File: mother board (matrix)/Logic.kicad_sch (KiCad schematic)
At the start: 1 part, among them U1 STM32F030C6Tx

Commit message: changes
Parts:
- added C1, C2, C3, C4: 100n, symbol Device:C
- added C304, C305: 20p, Capacitor_SMD:C_0603_1608Metric_Pad1.08x0.95mm_HandSolder, symbol Device:C_Small
- added C306, C308: 10u, Capacitor_Tantalum_SMD:CP_EIA-6032-28_Kemet-C_Pad2.25x2.35mm_HandSolder, symbol Device:C_Polarized_Small
- added C307, C309: 100n, Capacitor_SMD:C_0603_1608Metric_Pad1.08x0.95mm_HandSolder, symbol Device:C_Small
- added D1, D2: D_TVS, symbol Device:D_TVS
- added D332: Green, LED_SMD:LED_0805_2012Metric_Pad1.15x1.40mm_HandSolder, symbol Device:LED_Small
- added D333: Red, LED_SMD:LED_0805_2012Metric_Pad1.15x1.40mm_HandSolder, symbol Device:LED_Small
- added J301: RS485, Connector_PinSocket_2.54mm:PinSocket_1x03_P2.54mm_Vertical_SMD_Pin1Right, symbol Connector_Generic:Conn_01x03
- added J304: SWD, Connector_PinSocket_2.54mm:PinSocket_1x04_P2.54mm_Vertical_SMD_Pin1Right, symbol Connector_Generic:Conn_01x04
- added J305: BOOT_TO/ SELECTOR, Connector_PinHeader_2.54mm:PinHeader_1x03_P2.54mm_Vertical_SMD_Pin1Left, symbol Connector_Generic:Conn_01x03
- added J311: BOOT_TO/ SELECTOR, Connector_PinHeader_2.54mm:PinHeader_1x02_P2.54mm_Vertical_SMD_Pin1Left, symbol Connector_Generic:Conn_01x02
- added R1, R2: 10, symbol Device:R
- added R3: 120, symbol Device:R
- added R301, R305, R309, R310, R311: 10k, Resistor_SMD:R_0603_1608Metric_Pad0.98x0.95mm_HandSolder, symbol Device:R_Small
- added R312: 510, Resistor_SMD:R_0603_1608Metric_Pad0.98x0.95mm_HandSolder, symbol Device:R_Small
- added R313: 680, Resistor_SMD:R_0603_1608Metric_Pad0.98x0.95mm_HandSolder, symbol Device:R_Small
- added R4: 360, symbol Device:R
- added SW301: SW_SPST, Button_Switch_SMD:SW_SPST_EVQPE1, symbol Switch:SW_SPST
- added U2: SN65HVD11HD, Package_SO:SOIC-8_3.9x4.9mm_P1.27mm, symbol Interface_UART:SN65HVD11HD
- added U302: LM1117-3.3, Package_TO_SOT_SMD:SOT-223, symbol Regulator_Linear:LM1117-3.3
- added Y301: 8 MHz, Crystal:Crystal_SMD_Abracon_ABM3C-4Pin_5.0x3.2mm, symbol Device:Crystal_Small
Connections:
- net at U1.1 (VDD): now also U1.24 (VDD), U1.48 (VDD), U1.9 (VDDA), C1.1, C2.1, C3.1, C4.1
- net GNDD: now reaches U1.23 (VSS), U1.47 (VSS)
- net GNDD: now also U1.8 (VSSA), C1.2, C2.2, C3.2, C304.1, C305.1, C306.2, C307.2, C308.2, C309.2, C4.2, D1.2 (A2), D2.2 (A2), D332.1 (K), D333.1 (K), J301.1 (Pin_1), J304.1 (Pin_1), J305.1 (Pin_1), J311.2 (Pin_2), R310.2, R311.2, R4.2, SW301.1 (A), U302.1 (GND), Y301.2 (GND), Y301.4 (GND)
- new net: C305.2, Y301.1
- new net: D1.1 (A1), J301.3 (Pin_3), R1.1, R3.1, R4.1
- new net: D2.1 (A1), J301.2 (Pin_2), R2.1, R3.2
- new net: J305.2 (Pin_2), R301.2
- new net: D333.2 (A), R313.2
- new net: D332.2 (A), R312.2
- new net +3.3V: C307.1, C308.1, C309.1, J304.4 (Pin_4), J305.3 (Pin_3), R305.1, R309.1, U302.2 (VO), U302.4 (VO)
- new net +5V: C306.1, J311.1 (Pin_1), U302.3 (VI)
- new net BOOT0: R301.1
- new net DE: R311.1
- new net LED_debug1: R312.1
- new net LED_debug2: R313.1
- new net RST: R305.2, SW301.2 (B)
- new net SWD_CLK: J304.2 (Pin_2)
- new net SWD_O: J304.3 (Pin_3)
- new net UART1_RX_R: R309.2
- new net Xtal_IN: C304.2, Y301.3
- new net ~{RE}: R310.1
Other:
- note added: "3.3V Regulation"
- note added: "DB BOOT SELECTOR"
- note added: "DB ICSP"
- note added: "DB Supply"
- note added: "Debug_LED"
- note added: "Doughter Board (LOGICAL BOARD)"
- note added: "INNY SYMBOL BYL, NIE WIEM CZY TEN NA PEWNO MOZE BYC"
- note added: "MCU"
- note added: "POWER DECOUPLING"
- note added: "max ESR 22 Ohm"
- moved on the sheet: U1

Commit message: matrix done
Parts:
- removed C1, C2, C3, C4: 100n, symbol Device:C
- removed C304, C305: 20p, Capacitor_SMD:C_0603_1608Metric_Pad1.08x0.95mm_HandSolder, symbol Device:C_Small
- removed C306, C308: 10u, Capacitor_Tantalum_SMD:CP_EIA-6032-28_Kemet-C_Pad2.25x2.35mm_HandSolder, symbol Device:C_Polarized_Small
- removed C307, C309: 100n, Capacitor_SMD:C_0603_1608Metric_Pad1.08x0.95mm_HandSolder, symbol Device:C_Small
- removed D1, D2: D_TVS, symbol Device:D_TVS
- removed D332: Green, LED_SMD:LED_0805_2012Metric_Pad1.15x1.40mm_HandSolder, symbol Device:LED_Small
- removed D333: Red, LED_SMD:LED_0805_2012Metric_Pad1.15x1.40mm_HandSolder, symbol Device:LED_Small
- removed J301: RS485, Connector_PinSocket_2.54mm:PinSocket_1x03_P2.54mm_Vertical_SMD_Pin1Right, symbol Connector_Generic:Conn_01x03
- removed J304: SWD, Connector_PinSocket_2.54mm:PinSocket_1x04_P2.54mm_Vertical_SMD_Pin1Right, symbol Connector_Generic:Conn_01x04
- removed J305: BOOT_TO/ SELECTOR, Connector_PinHeader_2.54mm:PinHeader_1x03_P2.54mm_Vertical_SMD_Pin1Left, symbol Connector_Generic:Conn_01x03
- removed J311: BOOT_TO/ SELECTOR, Connector_PinHeader_2.54mm:PinHeader_1x02_P2.54mm_Vertical_SMD_Pin1Left, symbol Connector_Generic:Conn_01x02
- removed R1, R2: 10, symbol Device:R
- removed R3: 120, symbol Device:R
- removed R301, R305, R309, R310, R311: 10k, Resistor_SMD:R_0603_1608Metric_Pad0.98x0.95mm_HandSolder, symbol Device:R_Small
- removed R312: 510, Resistor_SMD:R_0603_1608Metric_Pad0.98x0.95mm_HandSolder, symbol Device:R_Small
- removed R313: 680, Resistor_SMD:R_0603_1608Metric_Pad0.98x0.95mm_HandSolder, symbol Device:R_Small
- removed R4: 360, symbol Device:R
- removed SW301: SW_SPST, Button_Switch_SMD:SW_SPST_EVQPE1, symbol Switch:SW_SPST
- removed U1: STM32F030C6Tx, Package_QFP:LQFP-48_7x7mm_P0.5mm, symbol MCU_ST_STM32F0:STM32F030C6Tx
- removed U2: SN65HVD11HD, Package_SO:SOIC-8_3.9x4.9mm_P1.27mm, symbol Interface_UART:SN65HVD11HD
- removed U302: LM1117-3.3, Package_TO_SOT_SMD:SOT-223, symbol Regulator_Linear:LM1117-3.3
- removed Y301: 8 MHz, Crystal:Crystal_SMD_Abracon_ABM3C-4Pin_5.0x3.2mm, symbol Device:Crystal_Small
- added C1, C2: 220u, Capacitor_SMD:CP_Elec_8x10.5, symbol Device:C_Polarized_Small
- added C3, C4, C5, C6: 100n, Capacitor_SMD:C_0603_1608Metric_Pad1.08x0.95mm_HandSolder, symbol Device:C_Small
- added J1: POWER, TerminalBlock:TerminalBlock_bornier-4_P5.08mm, symbol Connector:Screw_Terminal_01x04
- added J2: DATA IN, Connector_PinSocket_2.54mm:PinSocket_1x04_P2.54mm_Vertical_SMD_Pin1Right, symbol Connector_Generic:Conn_01x04
- added J3: Serial_BUS, Connector_PinSocket_2.54mm:PinSocket_1x04_P2.54mm_Vertical_SMD_Pin1Right, symbol Connector_Generic:Conn_01x04
- added J4: OUTPUT, Connector_PinHeader_2.54mm:PinHeader_2x05_P2.54mm_Vertical_SMD, symbol Connector_Generic:Conn_02x05_Odd_Even
- added J5: INPUT, Connector_PinHeader_2.54mm:PinHeader_2x05_P2.54mm_Vertical_SMD, symbol Connector_Generic:Conn_02x05_Odd_Even
- added J6: DATA OUT, Connector_PinSocket_2.54mm:PinSocket_1x04_P2.54mm_Vertical_SMD_Pin1Right, symbol Connector_Generic:Conn_01x04
- added R1: R_red, Resistor_SMD:R_0805_2012Metric_Pad1.20x1.40mm_HandSolder, symbol Device:R_Small
- added R2: R_green, Resistor_SMD:R_0805_2012Metric_Pad1.20x1.40mm_HandSolder, symbol Device:R_Small
- added R3: R_blue, Resistor_SMD:R_0805_2012Metric_Pad1.20x1.40mm_HandSolder, symbol Device:R_Small
- added TP1, TP2, TP3, TP4, TP5, TP6: TestPoint, TestPoint:TestPoint_Pad_1.0x1.0mm, symbol Connector:TestPoint
- added U1, U2, U3: SM16206, Package_SO:SSOP-24_3.9x8.7mm_P0.635mm, symbol SM16206:SM16206
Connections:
- net +5V: now also C1.1, C2.1, C3.1, C4.1, C5.1, C6.1, J1.3 (Pin_3), J1.4 (Pin_4), TP1.1, U1.24 (VDD), U2.24 (VDD), U3.24 (VDD)
- new net: TP6.1, U2.22 (SDO), U3.2 (SDI)
- new net: TP5.1, U1.22 (SDO), U2.2 (SDI)
- new net B_Row0: U3.5 (OUT0)
- new net B_Row1: U3.6 (OUT1)
- new net B_Row10: U3.15 (OUT10)
- new net B_Row11: U3.16 (OUT11)
- new net B_Row12: U3.17 (OUT12)
- new net B_Row2: U3.7 (OUT2)
- new net B_Row3: U3.8 (OUT3)
- new net B_Row4: U3.9 (OUT4)
- new net B_Row5: U3.10 (OUT5)
- new net B_Row6: U3.11 (OUT6)
- new net B_Row7: U3.12 (OUT7)
- new net B_Row8: U3.13 (OUT8)
- new net B_Row9: U3.14 (OUT9)
- new net Col0: J4.8 (Pin_8), J5.8 (Pin_8)
- new net Col1: J4.7 (Pin_7), J5.7 (Pin_7)
- new net Col2: J4.9 (Pin_9), J5.9 (Pin_9)
- new net Col3: J4.10 (Pin_10), J5.10 (Pin_10)
- new net Col4: J4.5 (Pin_5), J5.5 (Pin_5)
- new net Col5: J4.6 (Pin_6), J5.6 (Pin_6)
- new net Col6: J4.4 (Pin_4), J5.4 (Pin_4)
- new net Col7: J4.3 (Pin_3), J5.3 (Pin_3)
- new net Col8: J4.2 (Pin_2), J5.2 (Pin_2)
- new net Col9: J4.1 (Pin_1), J5.1 (Pin_1)
- new net GND: C1.2, C2.2, C3.2, C4.2, C5.2, C6.2, J1.1 (Pin_1), J1.2 (Pin_2), J2.4 (Pin_4), J3.4 (Pin_4), J6.4 (Pin_4), R1.2, R2.2, R3.2, U1.1 (GND), U1.21 (~{OE}), U2.1 (GND), U2.21 (~{OE}), U3.1 (GND), U3.21 (~{OE})
- new net G_Row0: U2.5 (OUT0)
- new net G_Row1: U2.6 (OUT1)
- new net G_Row10: U2.15 (OUT10)
- new net G_Row11: U2.16 (OUT11)
- new net G_Row12: U2.17 (OUT12)
- new net G_Row2: U2.7 (OUT2)
- new net G_Row3: U2.8 (OUT3)
- new net G_Row4: U2.9 (OUT4)
- new net G_Row5: U2.10 (OUT5)
- new net G_Row6: U2.11 (OUT6)
- new net G_Row7: U2.12 (OUT7)
- new net G_Row8: U2.13 (OUT8)
- new net G_Row9: U2.14 (OUT9)
- new net R_Bset: R3.1, TP4.1, U3.23 (R-EXT)
- new net R_Gset: R2.1, TP3.1, U2.23 (R-EXT)
- new net R_Row0: U1.5 (OUT0)
- new net R_Row1: U1.6 (OUT1)
- new net R_Row10: U1.15 (OUT10)
- new net R_Row11: U1.16 (OUT11)
- new net R_Row12: U1.17 (OUT12)
- new net R_Row2: U1.7 (OUT2)
- new net R_Row3: U1.8 (OUT3)
- new net R_Row4: U1.9 (OUT4)
- new net R_Row5: U1.10 (OUT5)
- new net R_Row6: U1.11 (OUT6)
- new net R_Row7: U1.12 (OUT7)
- new net R_Row8: U1.13 (OUT8)
- new net R_Row9: U1.14 (OUT9)
- new net R_Rset: R1.1, TP2.1, U1.23 (R-EXT)
- new net SDO: J6.1 (Pin_1), U3.22 (SDO)
- new net S_CLK: J2.2 (Pin_2), J3.2 (Pin_2), J6.2 (Pin_2), U1.3 (CLK), U2.3 (CLK), U3.3 (CLK)
- new net S_DATA: J2.1 (Pin_1), J3.1 (Pin_1), U1.2 (SDI)
- new net S_LE: J2.3 (Pin_3), J3.3 (Pin_3), J6.3 (Pin_3), U1.4 (LE), U2.4 (LE), U3.4 (LE)
- no-connect marks 0 -> 9
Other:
- note added: "BLUE"
- note added: "Column pass through"
- note added: "GREEN"
- note added: "Mother Board"
- note added: "POWER INPUT"
- note added: "RED"
- note added: "Serial Bus MB INPUT"
- note added: "Serial Bus MB MASTER Connector"
- note added: "Serial Bus MB Output"
- note removed: "3.3V Regulation"
- note removed: "DB BOOT SELECTOR"
- note removed: "DB ICSP"
- note removed: "DB Supply"
- note removed: "Debug_LED"
- note removed: "Doughter Board (LOGICAL BOARD)"
- note removed: "INNY SYMBOL BYL, NIE WIEM CZY TEN NA PEWNO MOZE BYC"
- note removed: "MCU"
- note removed: "POWER DECOUPLING"
- note removed: "max ESR 22 Ohm"

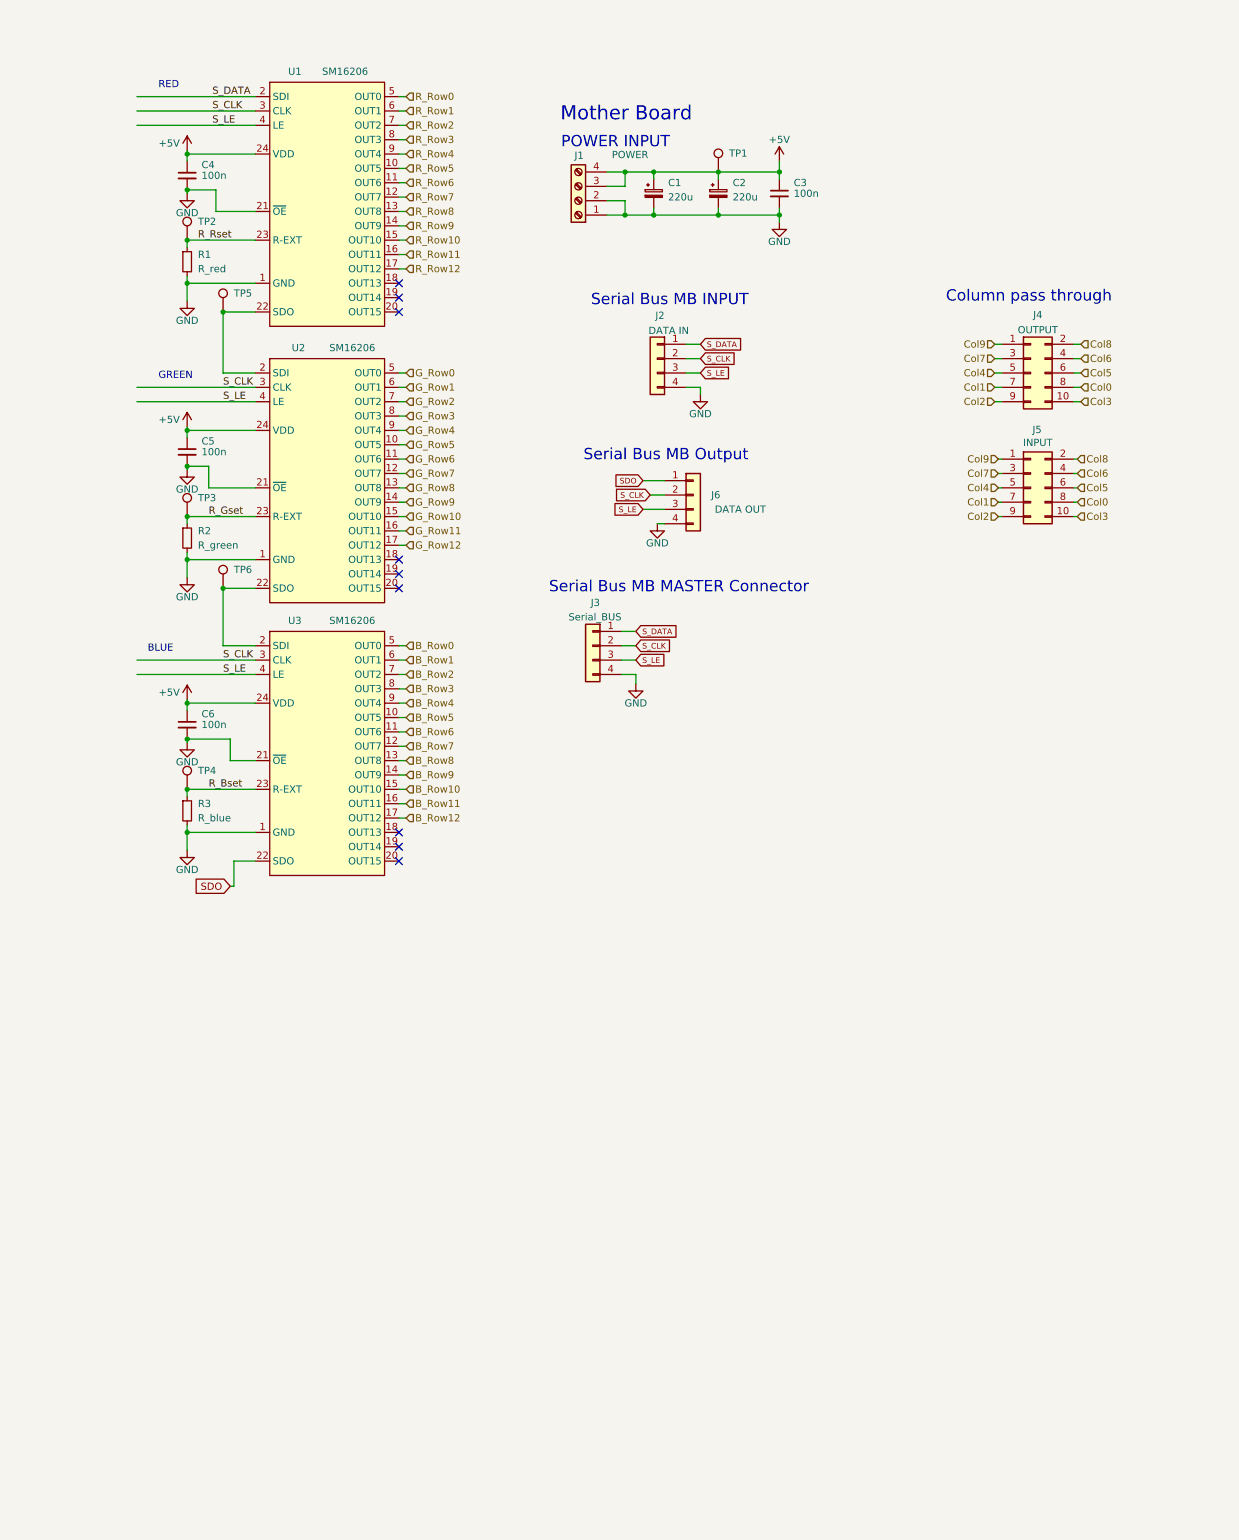
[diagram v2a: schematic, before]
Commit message: Fixed GND planes and rerouted bottom layer signals
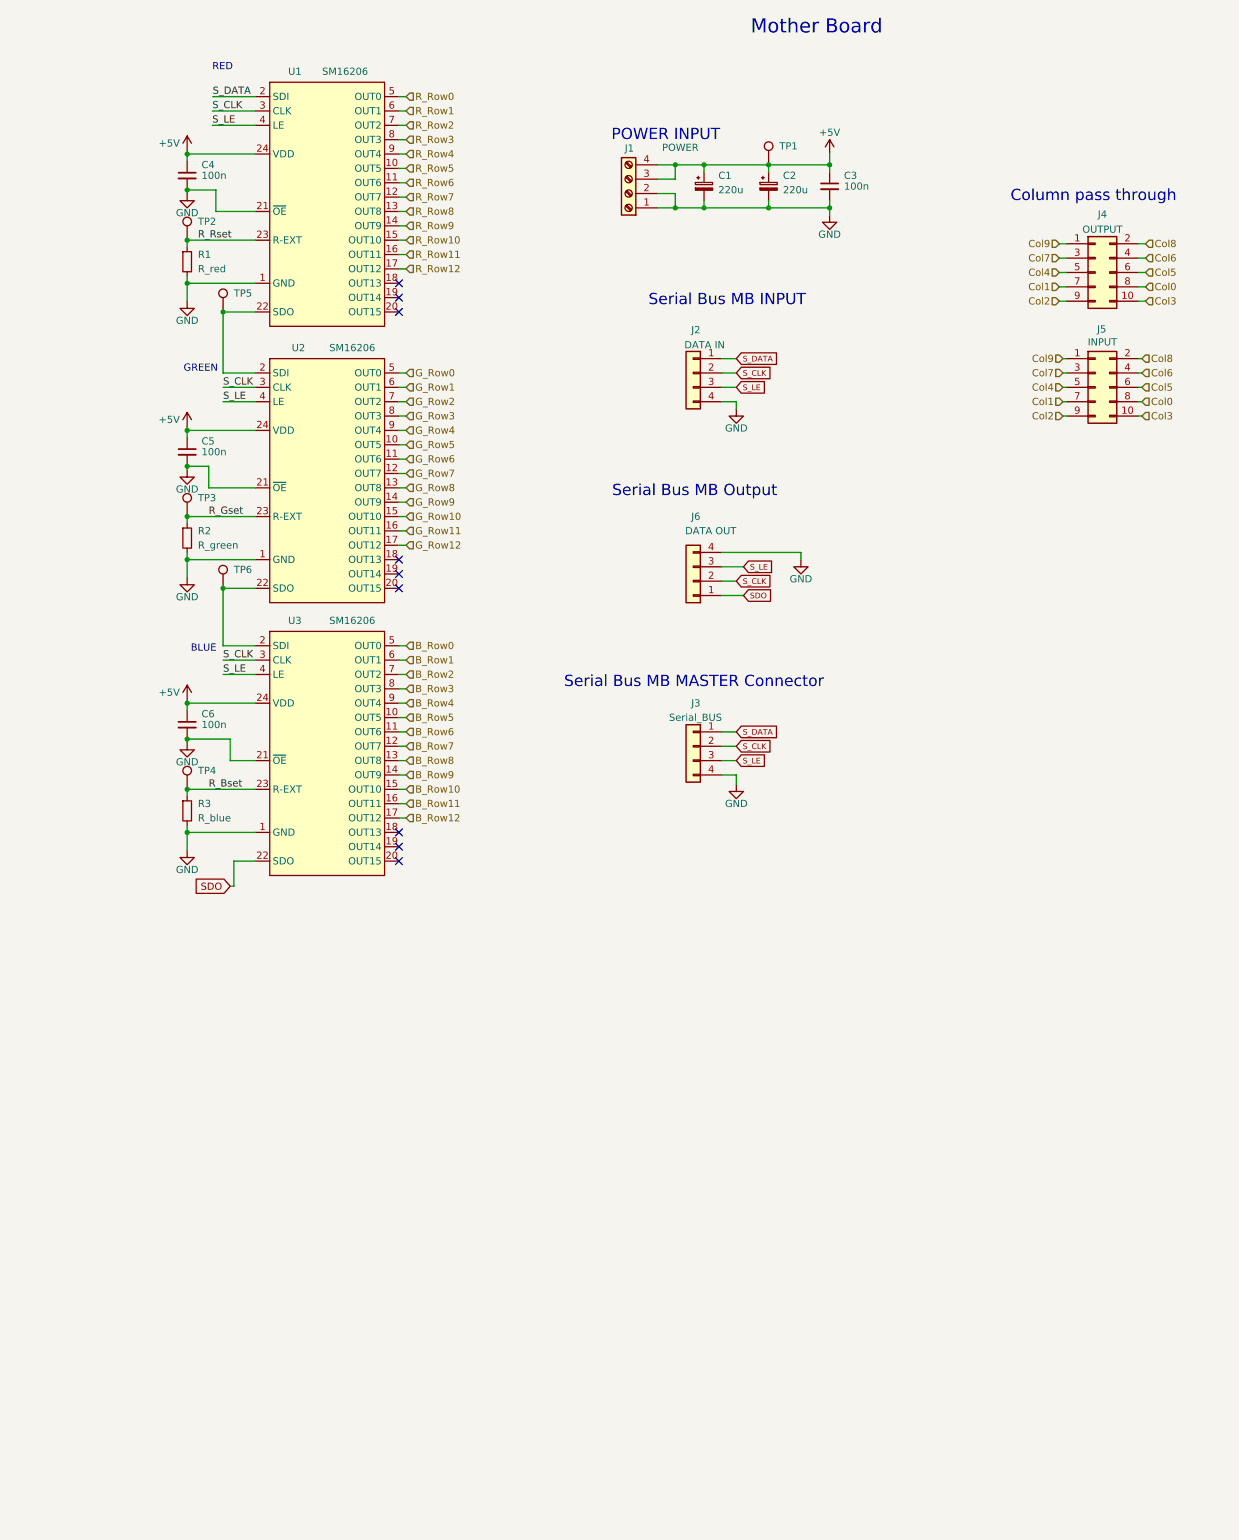
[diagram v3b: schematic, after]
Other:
- moved on the sheet: C1, C2, C3, J1, J2, J3, J4, J5, J6, TP1
